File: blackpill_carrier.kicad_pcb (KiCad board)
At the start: 2 copper layers, 63.5 x 76.2 mm, 33 parts, among them J1 Conn_01x03, J2 FTSH-105-01-F-DV-K-P-TR, J3 Conn_ARM_JTAG_SWD_10, J4 PicoBlade, U1 BlackPill

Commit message: Initial layout and component updates
May require more work after testing is completed
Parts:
- removed U1: BlackPill, sjp_modules:Blackpill F411
- added J5: Conn_01x40_Socket, Connector_PinSocket_2.54mm:PinSocket_1x20_P2.54mm_Vertical, F.Cu at (118.4, 77.6)
- added J6: Conn_01x40_Socket, Connector_PinSocket_2.54mm:PinSocket_1x20_P2.54mm_Vertical, F.Cu at (133.6, 125.9)
- added J7: Conn_01x04_Socket, Connector_PinSocket_2.54mm:PinSocket_1x04_P2.54mm_Vertical, F.Cu at (122.2, 122.1)
- J1: footprint Connector_PinHeader_1.00mm:PinHeader_1x03_P1.00mm_Vertical_SMD_Pin1Right -> Connector_PinHeader_2.54mm:PinHeader_1x03_P2.54mm_Vertical_SMD_Pin1Right
- J2: footprint sjp_connectors:FTSH-105-XX-X-DV -> Connector_PinHeader_1.27mm:PinHeader_2x05_P1.27mm_Vertical_SMD
- J3: value Conn_ARM_JTAG_SWD_10 -> FTSH-105-01-F-DV-K-P-TR; footprint sjp_connectors:FTSH-105-XX-X-DV -> Connector_PinHeader_1.27mm:PinHeader_2x05_P1.27mm_Vertical_SMD
- turned J2 to 180 degrees
- turned J3 to 0 degrees
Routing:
- net +3V3: track 116.2 -> 117.1 mm
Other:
- board text added: "Blackpill as Blackmagic Probe Carrier Sid Price Design v1.1"
- board text removed: "Blackpill as Blackmagic Probe Carrier Sid Price Design v1.0"

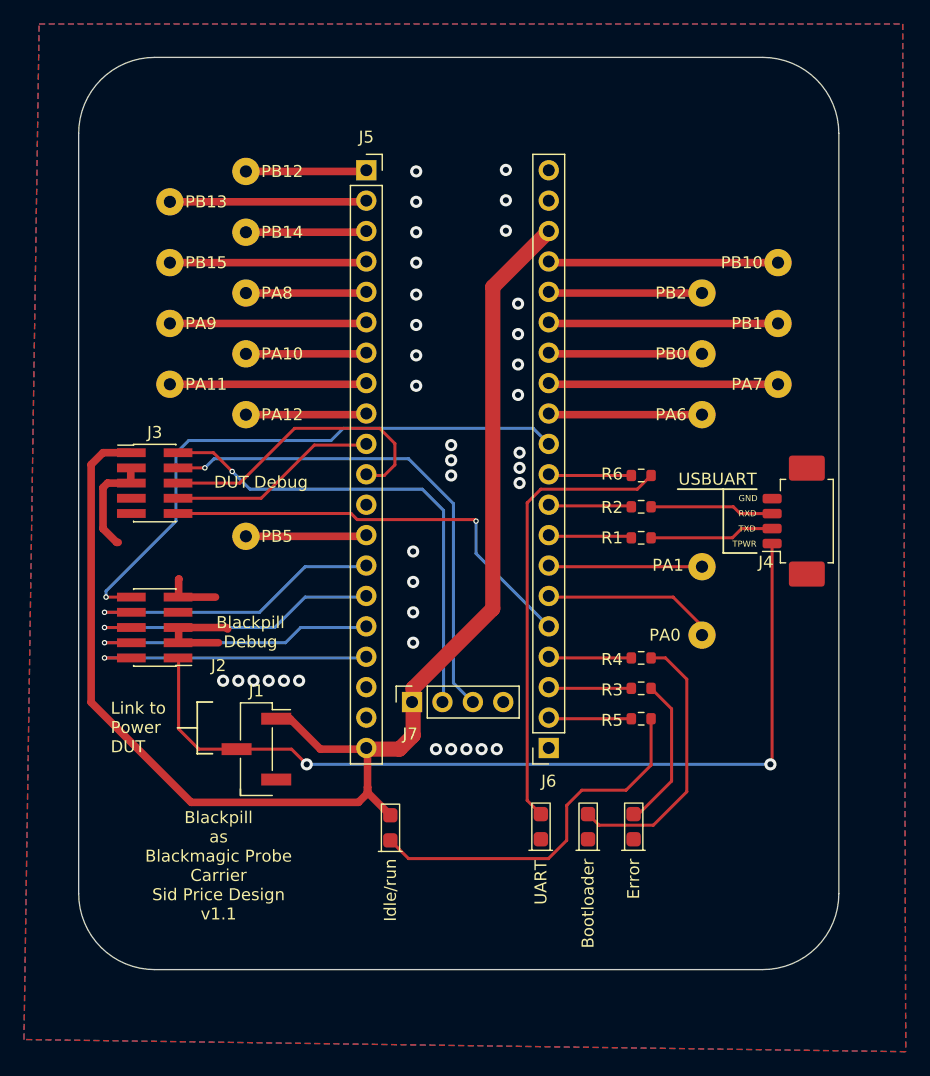
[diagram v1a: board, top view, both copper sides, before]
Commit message: Remove test points etc.
Removed all components not REQUIRED for BMF to operate.
Also removed unwanted jumper.
Changed footprint of target power selector.
Added pull-down for PA10
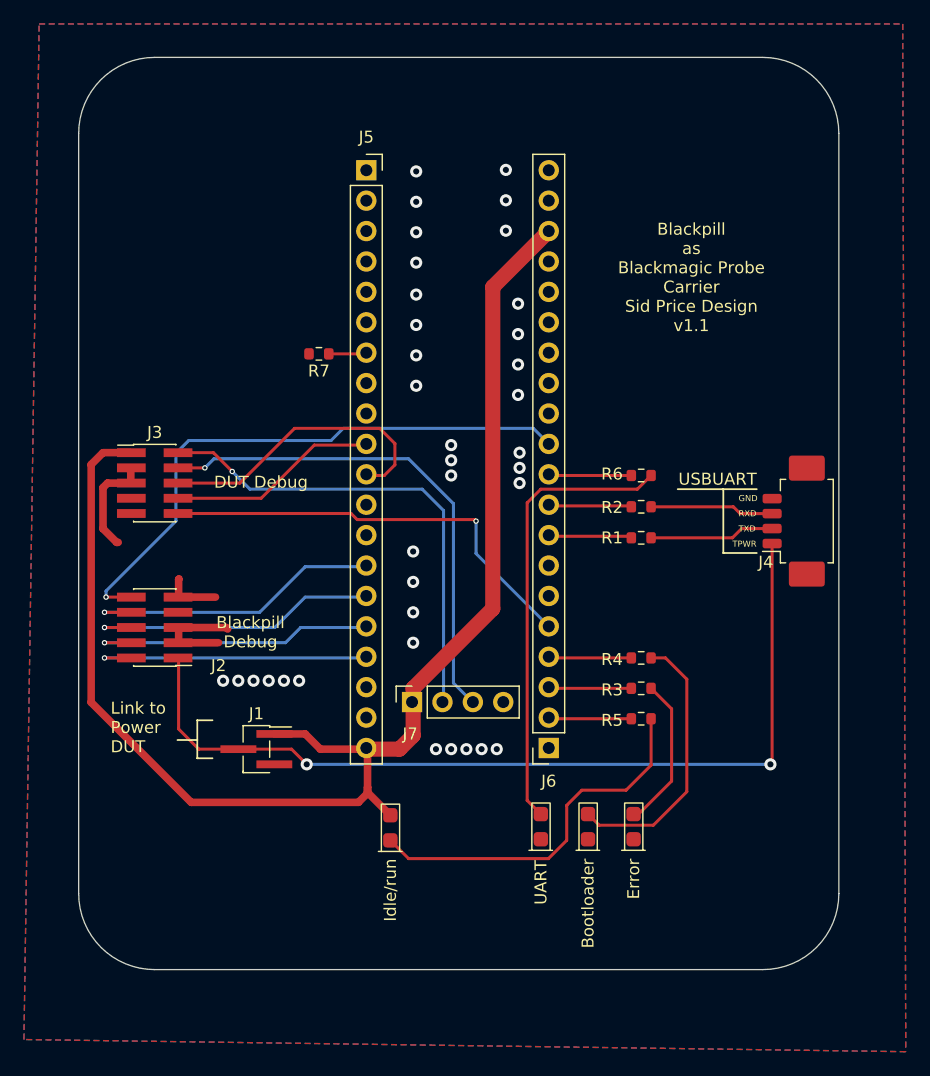
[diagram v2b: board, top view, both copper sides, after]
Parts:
- removed TP1, TP10, TP11, TP12, TP13, TP14, TP15, TP16, TP17, TP18, TP2, TP3, TP4, TP5, TP6, TP7, TP8, TP9: TestPoint, sjp_connectors:151-201-RC-Testpoint
- added R7: 10K, Resistor_SMD:R_0603_1608Metric, F.Cu at (114.4, 93.0)
- J1: value Conn_01x03 -> M50-3630342; footprint Connector_PinHeader_2.54mm:PinHeader_1x03_P2.54mm_Vertical_SMD_Pin1Right -> Connector_PinHeader_1.27mm:PinHeader_1x03_P1.27mm_Vertical_SMD_Pin1Right
- J5, J6: value Conn_01x40_Socket -> B-2200S20P-A120
- J7: value Conn_01x04_Socket -> B-2200S04P-A120
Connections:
- J5 pad 1: Net-(J5-Pin_1) -> unconnected-(J5-Pin_1-Pad1)
- J5 pad 13: Net-(J5-Pin_13) -> unconnected-(J5-Pin_13-Pad13)
- J5 pad 2: Net-(J5-Pin_2) -> unconnected-(J5-Pin_2-Pad2)
- J5 pad 3: Net-(J5-Pin_3) -> unconnected-(J5-Pin_3-Pad3)
- J5 pad 4: Net-(J5-Pin_4) -> unconnected-(J5-Pin_4-Pad4)
- J5 pad 5: Net-(J5-Pin_5) -> unconnected-(J5-Pin_5-Pad5)
- J5 pad 6: Net-(J5-Pin_6) -> unconnected-(J5-Pin_6-Pad6)
- J5 pad 8: Net-(J5-Pin_8) -> unconnected-(J5-Pin_8-Pad8)
- J5 pad 9: Net-(J5-Pin_9) -> unconnected-(J5-Pin_9-Pad9)
- J6 pad 12: Net-(J6-Pin_12) -> unconnected-(J6-Pin_12-Pad12)
- J6 pad 13: Net-(J6-Pin_13) -> unconnected-(J6-Pin_13-Pad13)
- J6 pad 14: Net-(J6-Pin_14) -> unconnected-(J6-Pin_14-Pad14)
- J6 pad 15: Net-(J6-Pin_15) -> unconnected-(J6-Pin_15-Pad15)
- J6 pad 16: Net-(J6-Pin_16) -> unconnected-(J6-Pin_16-Pad16)
- J6 pad 17: Net-(J6-Pin_17) -> unconnected-(J6-Pin_17-Pad17)
- J6 pad 6: Net-(J6-Pin_6) -> unconnected-(J6-Pin_6-Pad6)
- J6 pad 7: Net-(J6-Pin_7) -> unconnected-(J6-Pin_7-Pad7)
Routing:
- net Net-(J6-Pin_17): track 19.1 -> 0.00 mm
- net Net-(J6-Pin_15): track 19.1 -> 0.00 mm
- net Net-(J6-Pin_13): track 19.1 -> 0.00 mm
- net Net-(J5-Pin_8): track 16.5 -> 0.00 mm
- net Net-(J5-Pin_6): track 16.5 -> 0.00 mm
- net Net-(J5-Pin_4): track 16.5 -> 0.00 mm
- net Net-(J5-Pin_2): track 16.5 -> 0.00 mm
- net Net-(J6-Pin_6): track 14.5 -> 0.00 mm
- net Net-(J6-Pin_7): track 12.7 -> 0.00 mm
- net Net-(J6-Pin_16): track 12.7 -> 0.00 mm
- net Net-(J6-Pin_14): track 12.7 -> 0.00 mm
- net Net-(J6-Pin_12): track 12.7 -> 0.00 mm
- net Net-(J5-Pin_9): track 10.2 -> 0.00 mm
- net Net-(J5-Pin_5): track 10.2 -> 0.00 mm
- net Net-(J5-Pin_3): track 10.2 -> 0.00 mm
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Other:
- board text removed: "PA0"
- board text removed: "PA1"
- board text removed: "PA10"
- board text removed: "PA11"
- board text removed: "PA12"
- board text removed: "PA6"
- board text removed: "PA7"
- board text removed: "PA8"
- board text removed: "PA9"
- board text removed: "PB0"
- board text removed: "PB1"
- board text removed: "PB10"
- board text removed: "PB12"
- board text removed: "PB13"
- board text removed: "PB14"
- board text removed: "PB15"
- board text removed: "PB2"
- board text removed: "PB5"

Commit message: Update 3D model for connector and fix silkscreen
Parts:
- J2, J3: footprint Connector_PinHeader_1.27mm:PinHeader_2x05_P1.27mm_Vertical_SMD -> sjp_connectors:FTSH-105-XX-X-DV
- turned J2 to -90 degrees
- turned J3 to 90 degrees

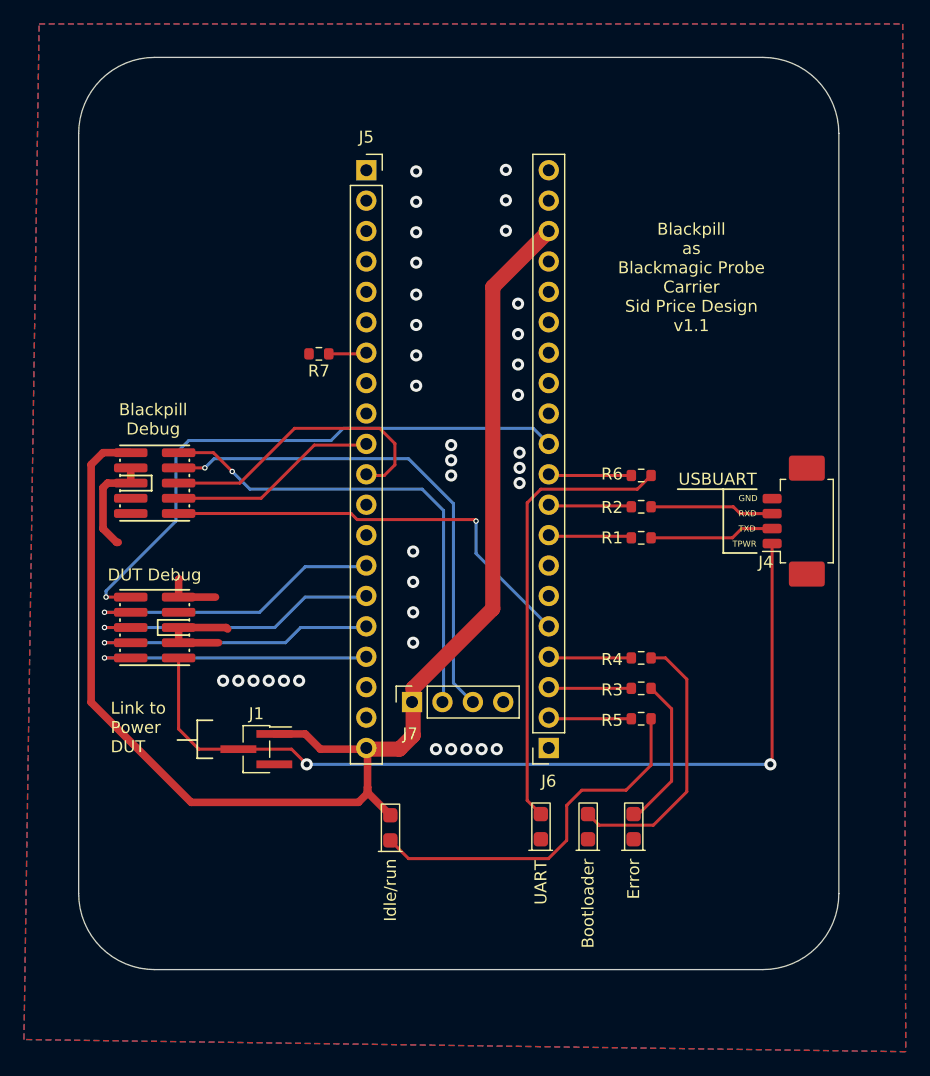
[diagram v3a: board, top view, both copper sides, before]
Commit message: Reduce size and re-arrange layout to look better.
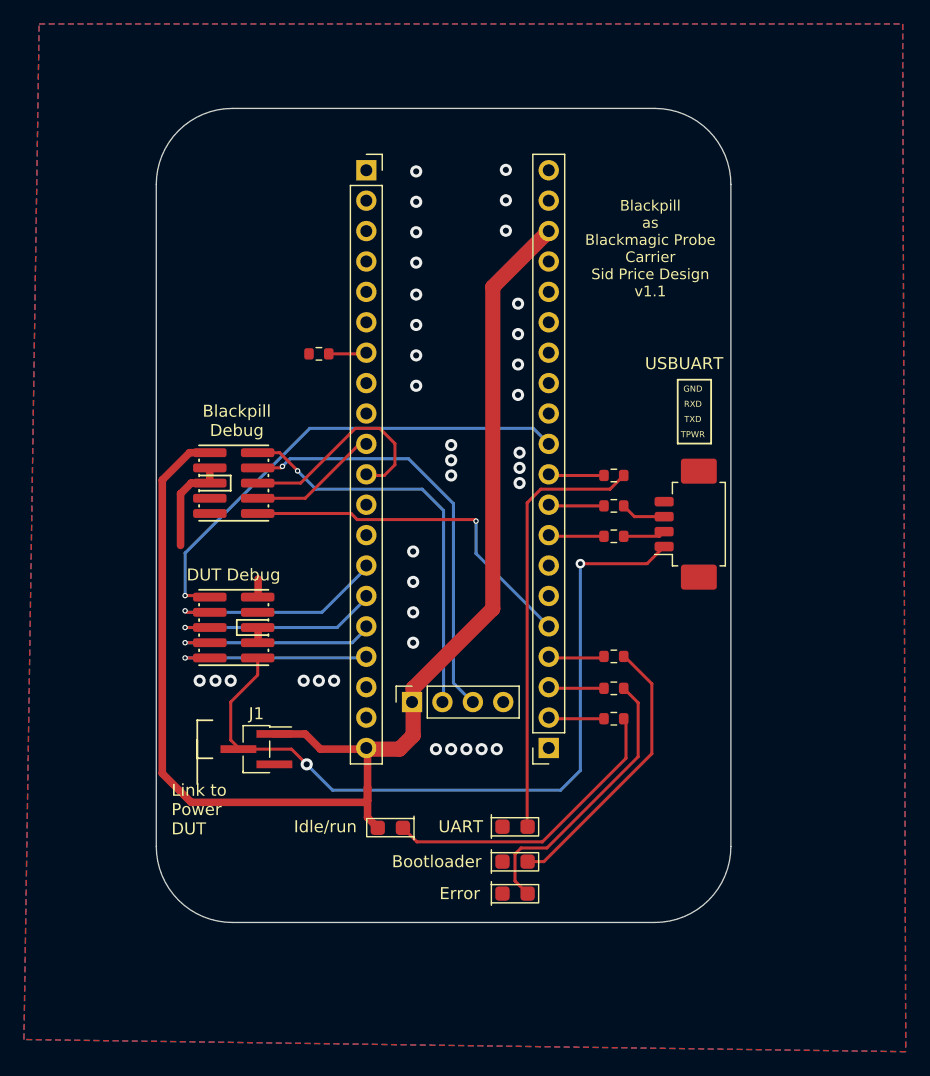
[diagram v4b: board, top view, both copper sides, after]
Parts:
- moved D1 11.4 mm to (130.8, 138.0), turned to 0 degrees
- moved J4 9.02 mm to (145.7, 107.2)
- moved D2 6.76 mm to (130.8, 135.4), turned to 0 degrees
- moved J2 6.60 mm to (107.3, 115.8)
- moved J3 6.60 mm to (107.3, 103.8)
- moved R1 2.29 mm to (139.1, 108.2)
- moved R4 2.29 mm to (139.1, 118.2)
- moved R2 2.29 mm to (139.1, 105.7)
- moved R3 2.29 mm to (139.1, 120.9)
- moved R5 2.29 mm to (139.1, 123.4)
- moved R6 2.29 mm to (139.1, 103.1)
- moved D4 2.16 mm to (130.8, 132.5), turned to 0 degrees
- turned D3 to 180 degrees
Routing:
- net GND: track 22.3 -> 11.2 mm
- net /TPWR: track 75.1 -> 64.3 mm
- net Net-(D1-A): track 12.9 -> 23.6 mm
- net /~{nRST}: track 49.2 -> 41.0 mm
- net /t_SWO/TDO: track 25.3 -> 18.4 mm
- net /t_SWDCLK/TCK: track 24.8 -> 17.8 mm
- net /t_NC/TDI: track 25.9 -> 19.0 mm
- net /t_SWDIO/TMS: track 24.2 -> 17.3 mm
- net Net-(J4-Pin_2): track 10.4 -> 3.72 mm
- net /~{RESET}: track 36.6 -> 30.0 mm
- net /b_TDI: track 17.6 -> 11.0 mm
- net /b_SWO: track 24.9 -> 18.3 mm
- net /b_SWDCLK: track 42.2 -> 35.6 mm
- net Net-(J4-Pin_3): track 10.3 -> 3.75 mm
- net /b_SWDIO: track 40.3 -> 33.7 mm
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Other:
- board size 63.5 x 76.2 mm -> 48 x 68 mm
